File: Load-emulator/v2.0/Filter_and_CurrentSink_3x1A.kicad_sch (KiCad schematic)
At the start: 11 parts, among them U1 LT1492, U4 INA185

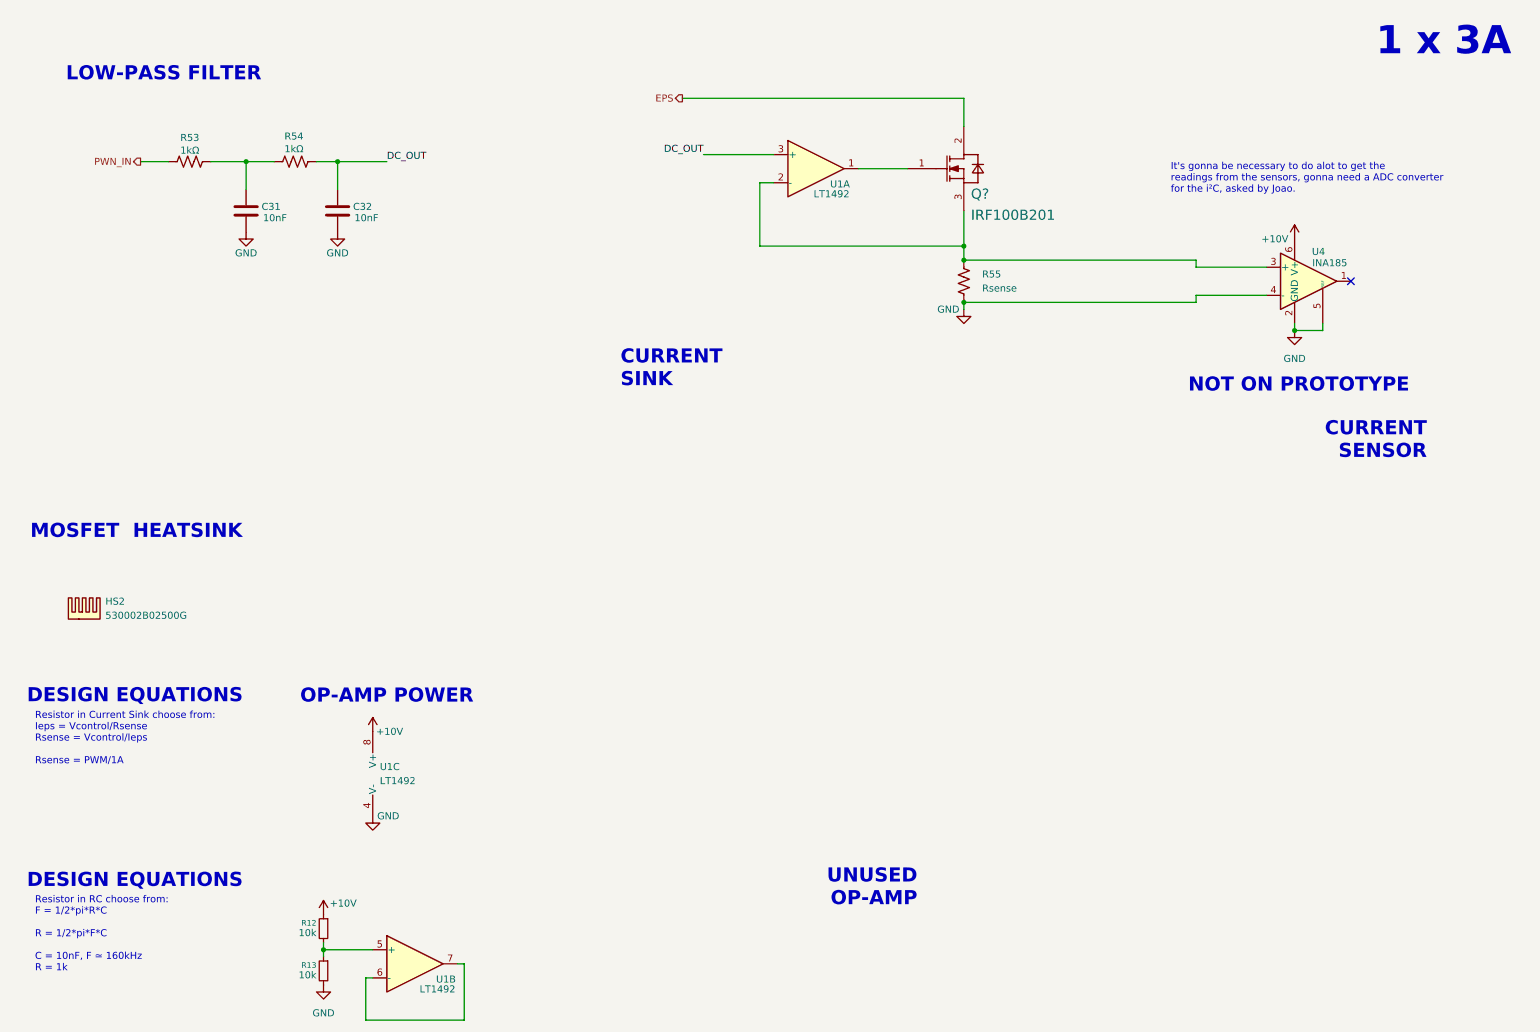
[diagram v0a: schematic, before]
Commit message: [v2.0 - WIP] Added PCB Sketch
[REMOVED]
 - Some comments;

[ADDED]
- 3D models for some components, like heatsinks;
- PCB Sketch (This is just to review how it will look);
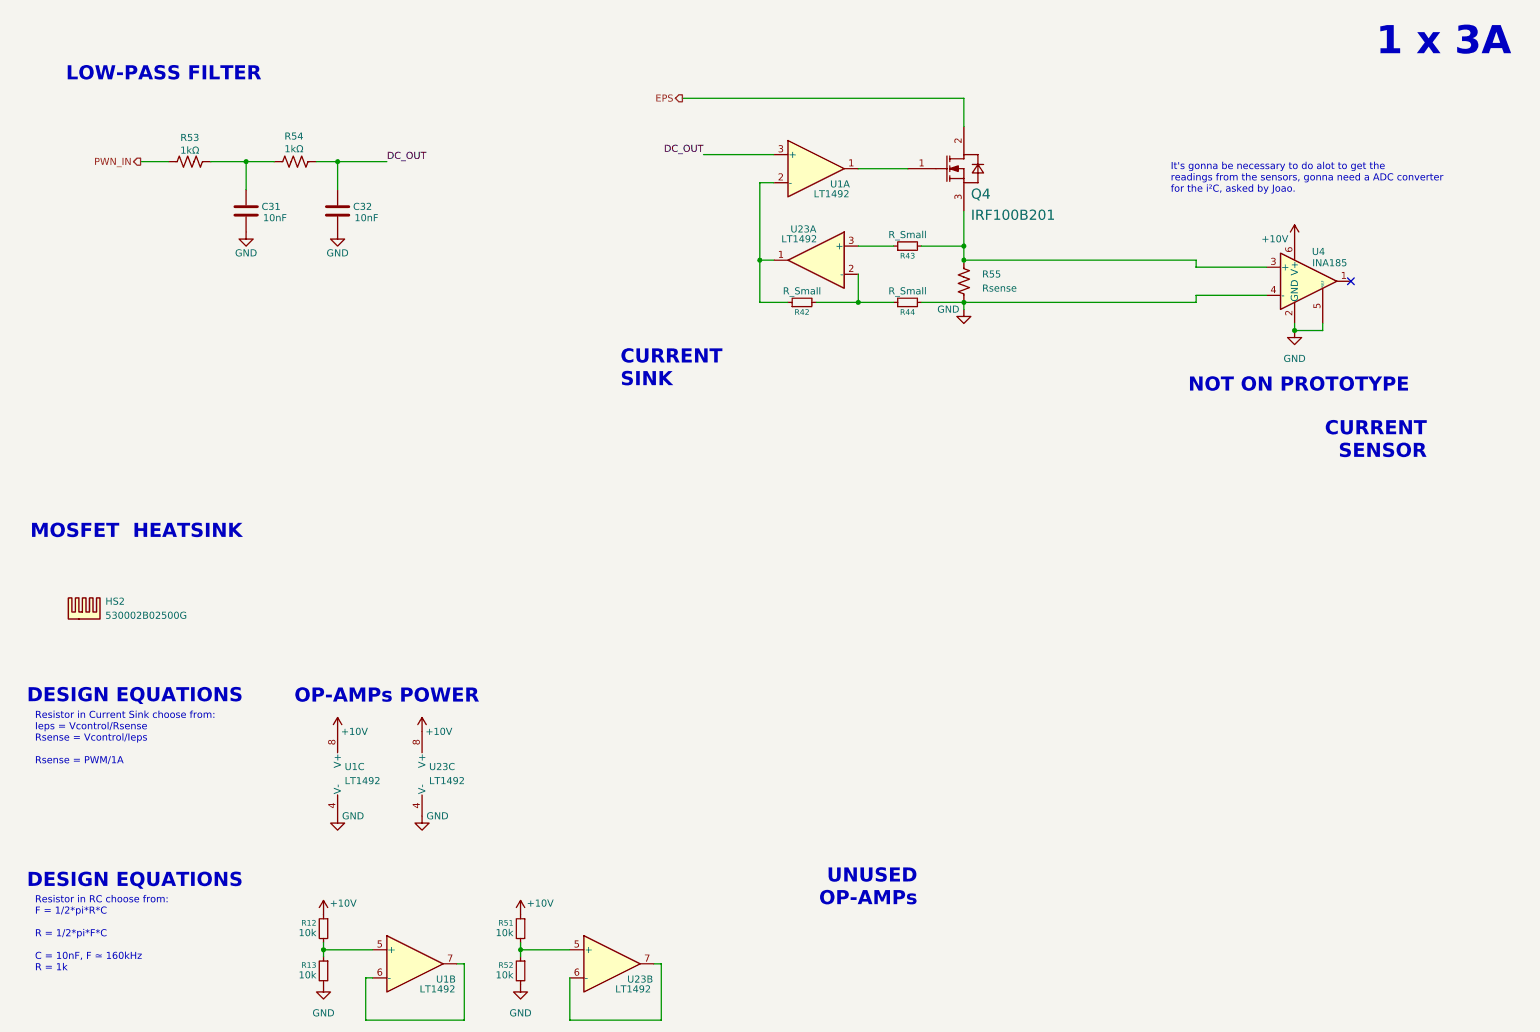
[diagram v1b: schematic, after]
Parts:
- added R42, R43, R44: R_Small, symbol Device:R_Small
- added R51, R52: 10k, Resistor_SMD:R_0603_1608Metric, symbol Device:R_Small
- added U23: LT1492, footprints:SO-8_S_LIT, symbol Amplifier_Operational:LT1492
- Q4: renamed from Q?; footprint (none) -> IFX-PG-TO220-3-904:IFX-PG-TO220-3-904
- R12, R13: footprint (none) -> Resistor_SMD:R_0603_1608Metric
- U1: footprint (none) -> footprints:SO-8_S_LIT; now in the parts list
- U1: footprint (none) -> footprints:SO-8_S_LIT
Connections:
- net +10V: now also R51.1, U23.8 (V+)
- net GND: now also R44.2, R52.2, U23.4 (V-)
- net at Q4.3 (SOURCE), R55.1, U4.3 (+): now also R43.2; no longer U1.2 (-)
- new net: R42.1, U1.2 (-), U23.1
- new net: R43.1, U23.3 (+)
- new net: R51.2, R52.1, U23.5 (+)
- new net: U23.6 (-), U23.7
- new net: R42.2, R44.1, U23.2 (-)
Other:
- note added: "OP-AMPs POWER"
- note added: "UNUSED OP-AMPs"
- note removed: "OP-AMP POWER"
- note removed: "UNUSED OP-AMP"
- moved on the sheet: U1C

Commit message: [v2.0 - WIP] Release Candidate 1. (#6)
Ready for review
- PCB Wired up.
- Schematic ready.

[MISSING]
- Values for some Resistors and Capacitors;
- Verify if EPS conector is correct;
- Change schematic to release.
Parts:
- removed U4: INA185, Package_TO_SOT_SMD:SOT-563, symbol Amplifier_Current:INA185
- added C3: C_Small, Capacitor_SMD:C_0805_2012Metric, symbol Device:C_Small
- added R7: R_Small, Resistor_SMD:R_0603_1608Metric, symbol Device:R_Small
- C1: renamed from C31; footprint Capacitor_SMD:C_0201_0603Metric -> Capacitor_SMD:C_0805_2012Metric
- C2: renamed from C32; footprint Capacitor_SMD:C_0201_0603Metric -> Capacitor_SMD:C_0805_2012Metric
- HS1: renamed from HS2; footprint (none) -> footprints:529802B02500G
- R1: renamed from R53; footprint Resistor_SMD:R_0201_0603Metric -> Resistor_SMD:R_0603_1608Metric
- R10: renamed from R44; footprint (none) -> Resistor_SMD:R_0603_1608Metric
- R11: renamed from R55; footprint (none) -> Resistor_SMD:R_2512_6332Metric
- R2: renamed from R54; footprint Resistor_SMD:R_0201_0603Metric -> Resistor_SMD:R_0603_1608Metric
- R8: renamed from R42; footprint (none) -> Resistor_SMD:R_0603_1608Metric
- R9: renamed from R43; footprint (none) -> Resistor_SMD:R_0603_1608Metric
- renumbered Q4 to Q1, R12 to R3, R13 to R4, R51 to R5, R52 to R6, U23 to U2
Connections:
- net at Q1.1 (GATE), U1.1: now also C3.2
- net at R8.1, U2.1: now also R7.1; no longer U1.2 (-)
- net GND renamed GNDPWR
- new net: C3.1, R7.2, U1.2 (-)
- no-connect marks 1 -> 0
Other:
- note added: "Resistor in Current Sink choose from: Rsense = (Vcontrol/Ieps)/10 Rsense = PWM/3A"
- note removed: "CURRENT SENSOR"
- note removed: "It's gonna be necessary to do alot to get the readings from the sensors, gonna need a ADC converter for the i²C, asked by Joao."
- note removed: "NOT ON PROTOTYPE"
- note removed: "Resistor in Current Sink choose from: Ieps = Vcontrol/Rsense Rsense = Vcontrol/Ieps Rsense = PWM/1A"
- moved on the sheet: Q1, R10, R11, R8, R9, U1A, U2A

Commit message: v2.0
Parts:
- C1, C2, C3, R1, R10, R11, R2, R3, R4, R5, R6, R7, R8, R9: Type (none) -> SMD
- HS1: Manufacturer (none) -> Boyd Laconia, LLC; Manufacturer Order Number (none) -> 530002B02500G; Type (none) -> Through Hole
- Q1: Type (none) -> Through Hole
- U1, U2: Manufacturer (none) -> Analog Devices Inc.; Manufacturer Order Number (none) -> LT1492CS8#TRPBF; Type (none) -> SMD
